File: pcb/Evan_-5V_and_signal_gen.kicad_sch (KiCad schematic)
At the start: 28 parts, among them IC1 TL7660IDGKR, IC4 UA78M33CDCYG3, IC9 TL081IDT, U5 TPS2069CDBVR_MOSFET

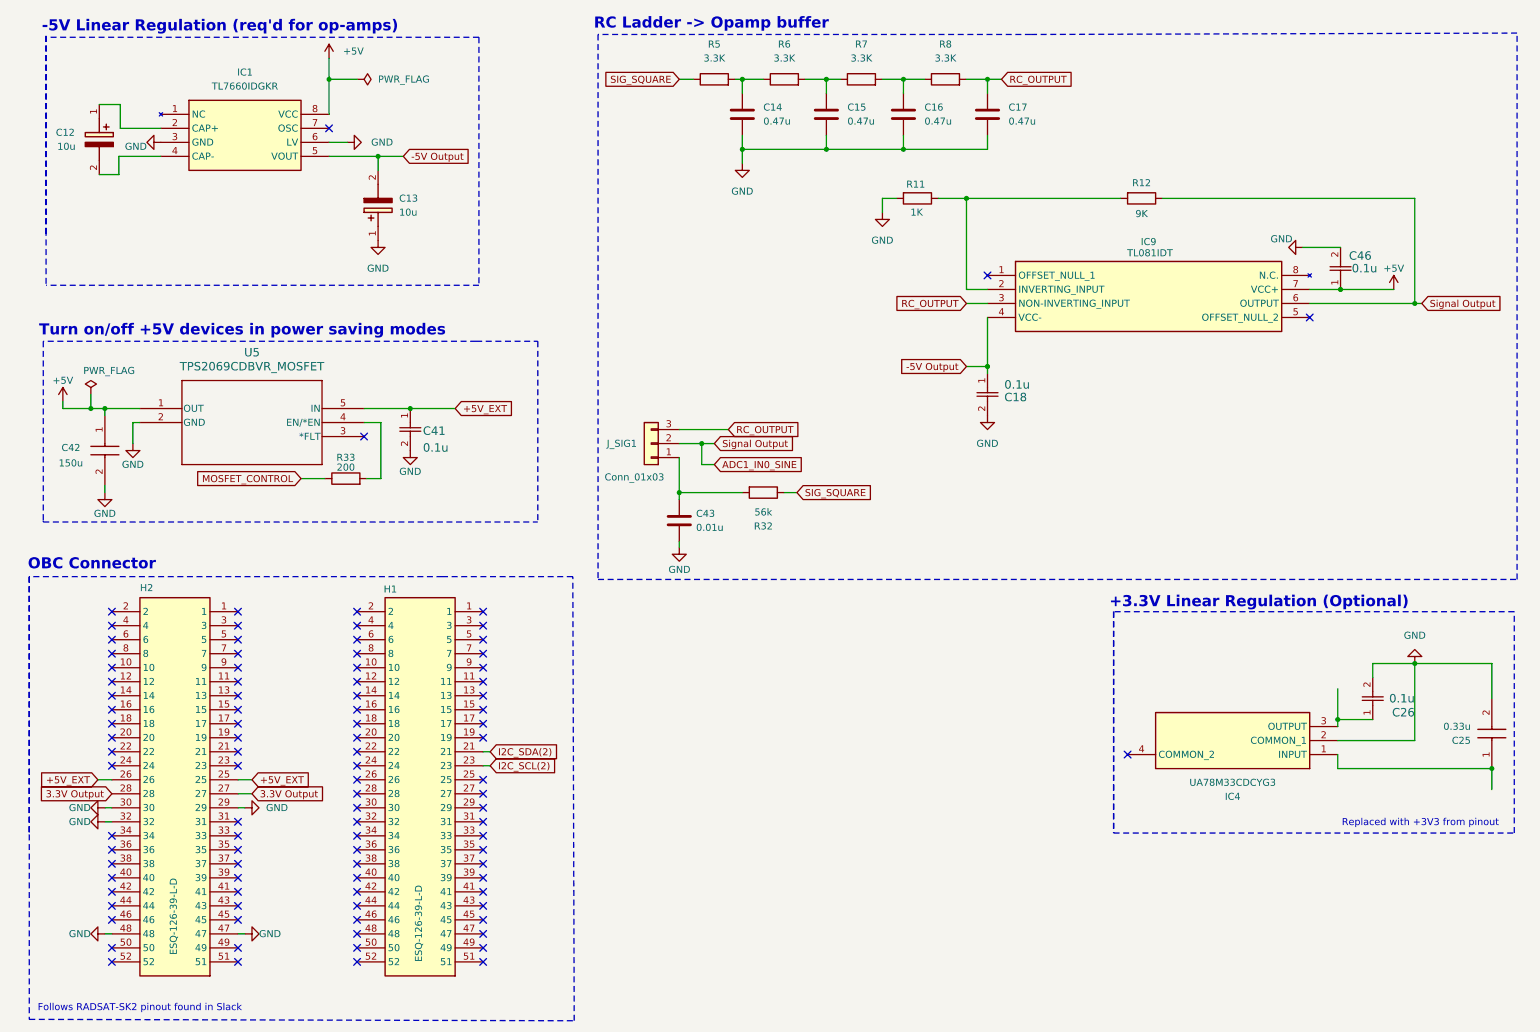
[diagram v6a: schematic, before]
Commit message: Added switchable inputs for opamps
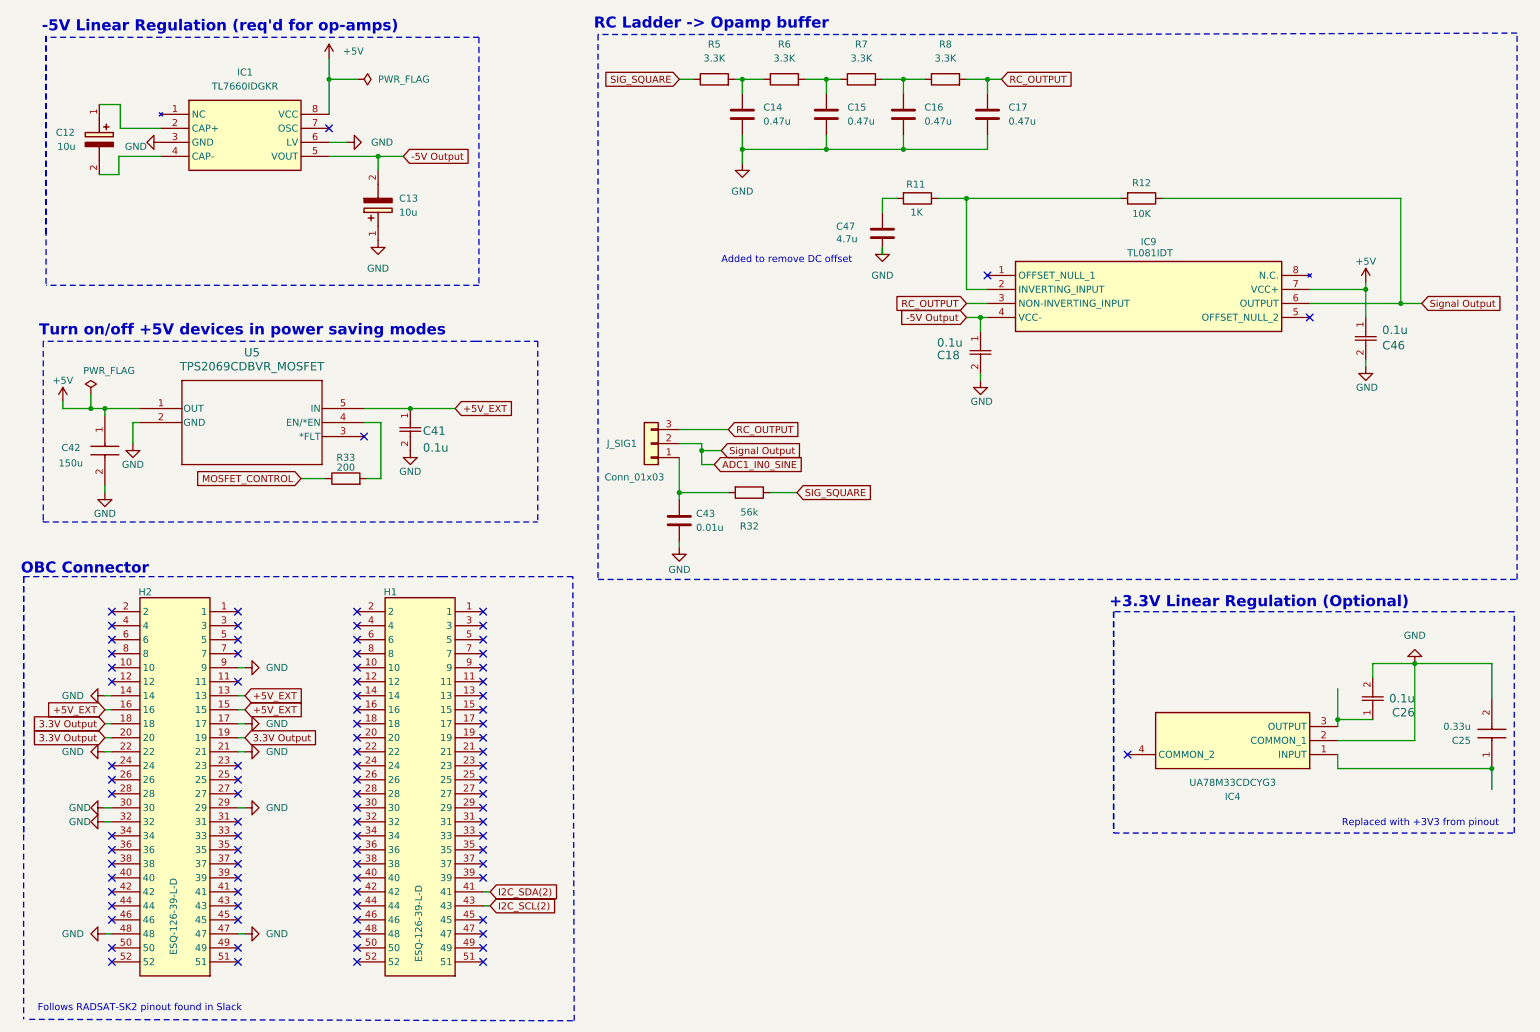
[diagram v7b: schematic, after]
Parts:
- added C47: 4.7u, Capacitor_SMD:C_0402_1005Metric, symbol Device:C
- C14, C15, C16, C17: footprint capstone:CAPC220145_88N_KEM-0.1u -> Capacitor_SMD:C_0402_1005Metric
- C43: footprint capstone:C0805 -> Capacitor_SMD:C_0402_1005Metric
- R12: value 9K -> 10K
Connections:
- net +5V_EXT: now also H2.13, H2.15, H2.16; no longer H2.25, H2.26
- net 3.3V Output: now also H2.18, H2.19, H2.20; no longer H2.27, H2.28
- net GND: now also H2.14, H2.17, H2.21, H2.22, H2.9, C47.2; no longer R11.2
- net I2C_SCL(2): now also H1.43; no longer H1.23
- net I2C_SDA(2): now also H1.41; no longer H1.21
- new net: C47.1, R11.2
- no-connect marks 98 -> 91
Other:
- note added: "Added to remove DC offset"
- moved on the sheet: C18, C46, R32

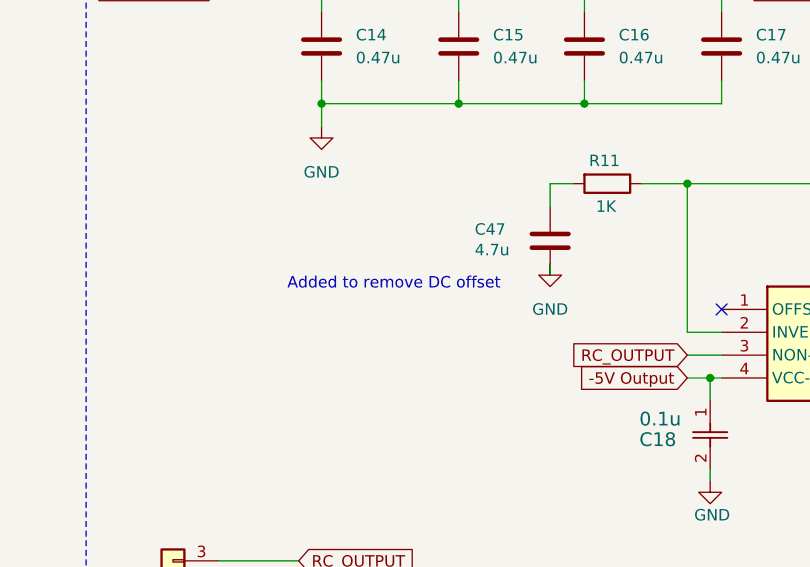
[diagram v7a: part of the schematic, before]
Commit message: Thermal Reliefs and Blind Vias
- Added back thermal reliefs to shields
- Swapped power vias to not be drilled across all layers
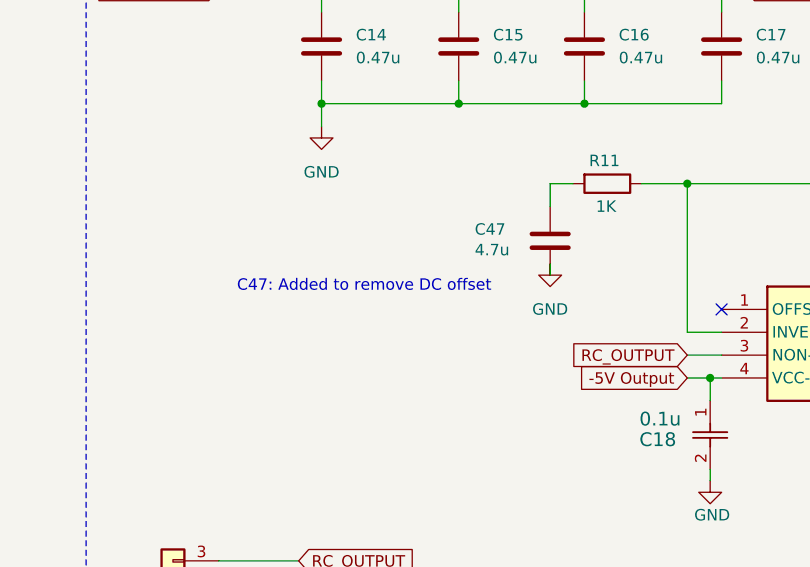
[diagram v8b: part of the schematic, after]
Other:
- note added: "C47: Added to remove DC offset"
- note removed: "Added to remove DC offset"
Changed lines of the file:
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@@
 		)
 	)
-	(text "Added to remove DC offset"
+	(text "C47: Added to remove DC offset"
 		(exclude_from_sim no)
-		(at 139.7 58.928 0)
+		(at 134.112 59.182 0)
 		(effects
 			(font
